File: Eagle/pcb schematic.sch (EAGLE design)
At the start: 17 parts

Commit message: PCB finita
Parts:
- BLUETOOTH: device SparkFun-Connectors:CONN_02 -> SparkFun-Connectors:CONN_04
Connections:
- net GND: now also BLUETOOTH.2
- net N$4: now also BLUETOOTH.4, PIN_123-124.1; no longer BLUETOOTH.1, PIN_123-124.2
- net N$6: now also BLUETOOTH.3, PIN_123-124.2; no longer BLUETOOTH.2, PIN_123-124.1
- net N$9: now also BLUETOOTH.1
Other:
- moved on the sheet: PIN_123-124
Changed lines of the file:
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@@
 <part name="R1" library="SparkFun-Resistors" deviceset="RESISTOR" device="AXIAL-0.3" value=" "/>
 <part name="PIN_123-124" library="SparkFun-Connectors" deviceset="CONN_02" device=""/>
-<part name="BLUETOOTH" library="SparkFun-Connectors" deviceset="CONN_02" device=""/>
 <part name="J1" library="SparkFun-Connectors" deviceset="CONN_02" device=""/>
+<part name="BLUETOOTH" library="SparkFun-Connectors" deviceset="CONN_04" device=""/>
 </parts>
 <sheets>
@@
 <attribute name="NAME" x="-10.16" y="61.976" size="1.778" layer="95" font="vector" rot="R180" align="bottom-center"/>
 </instance>
-<instance part="PIN_123-124" gate="G$1" x="-55.88" y="48.26" smashed="yes">
-<attribute name="VALUE" x="-58.42" y="43.434" size="1.778" layer="96" font="vector"/>
-<attribute name="NAME" x="-61.468" y="43.18" size="1.778" layer="95" font="vector" rot="R90"/>
-</instance>
-<instance part="BLUETOOTH" gate="G$1" x="-25.4" y="50.8" smashed="yes" rot="R180">
-<attribute name="VALUE" x="-22.86" y="55.626" size="1.778" layer="96" font="vector" rot="R180"/>
-<attribute name="NAME" x="-22.352" y="53.34" size="1.778" layer="95" font="vector" rot="R270"/>
+<instance part="PIN_123-124" gate="G$1" x="-55.88" y="45.72" smashed="yes">
+<attribute name="VALUE" x="-58.42" y="40.894" size="1.778" layer="96" font="vector"/>
+<attribute name="NAME" x="-61.468" y="40.64" size="1.778" layer="95" font="vector" rot="R90"/>
 </instance>
 <instance part="J1" gate="G$1" x="5.08" y="96.52" smashed="yes" rot="R270">
 <attribute name="VALUE" x="0.254" y="99.06" size="1.778" layer="96" font="vector" rot="R270"/>
 <attribute name="NAME" x="10.668" y="99.06" size="1.778" layer="95" font="vector" rot="R270"/>
+</instance>
+<instance part="BLUETOOTH" gate="G$1" x="17.78" y="50.8" smashed="yes" rot="R180">
+<attribute name="VALUE" x="22.86" y="58.166" size="1.778" layer="96" font="vector" rot="R180"/>
+<attribute name="NAME" x="23.368" y="55.88" size="1.778" layer="95" font="vector" rot="R270"/>
 </instance>
 </instances>
@@
 <wire x1="-48.26" y1="76.2" x2="5.08" y2="76.2" width="0.1524" layer="91"/>
 <pinref part="FLEX2" gate="G$1" pin="1"/>
-<wire x1="30.48" y1="76.2" x2="33.02" y2="76.2" width="0.1524" layer="91"/>
-<wire x1="33.02" y1="76.2" x2="45.72" y2="76.2" width="0.1524" layer="91"/>
 <wire x1="45.72" y1="20.32" x2="45.72" y2="76.2" width="0.1524" layer="91"/>
 <wire x1="45.72" y1="76.2" x2="60.96" y2="76.2" width="0.1524" layer="91"/>
@@
 <wire x1="60.96" y1="7.62" x2="60.96" y2="76.2" width="0.1524" layer="91"/>
 <junction x="60.96" y="76.2"/>
+<wire x1="5.08" y1="76.2" x2="12.7" y2="76.2" width="0.1524" layer="91"/>
+<junction x="5.08" y="76.2"/>
+<pinref part="BLUETOOTH" gate="G$1" pin="1"/>
+<wire x1="12.7" y1="76.2" x2="30.48" y2="76.2" width="0.1524" layer="91"/>
+<wire x1="30.48" y1="76.2" x2="45.72" y2="76.2" width="0.1524" layer="91"/>
+<wire x1="12.7" y1="53.34" x2="12.7" y2="76.2" width="0.1524" layer="91"/>
+<junction x="12.7" y="76.2"/>
 <pinref part="FLEX1" gate="G$1" pin="1"/>
 <wire x1="30.48" y1="35.56" x2="30.48" y2="76.2" width="0.1524" layer="91"/>
-<wire x1="5.08" y1="76.2" x2="30.48" y2="76.2" width="0.1524" layer="91"/>
-<junction x="5.08" y="76.2"/>
+<junction x="30.48" y="76.2"/>
 </segment>
 </net>
@@
 <pinref part="R1" gate="G$1" pin="2"/>
 <wire x1="-22.86" y1="63.5" x2="-15.24" y2="63.5" width="0.1524" layer="91"/>
-</segment>
-</net>
-<net name="N$4" class="0">
-<segment>
-<pinref part="PIN_123-124" gate="G$1" pin="2"/>
-<pinref part="BLUETOOTH" gate="G$1" pin="1"/>
-<wire x1="-48.26" y1="50.8" x2="-33.02" y2="50.8" width="0.1524" layer="91"/>
-</segment>
-</net>
-<net name="N$6" class="0">
-<segment>
-<pinref part="PIN_123-124" gate="G$1" pin="1"/>
-<pinref part="BLUETOOTH" gate="G$1" pin="2"/>
-<wire x1="-48.26" y1="48.26" x2="-33.02" y2="48.26" width="0.1524" layer="91"/>
 </segment>
 </net>
@@
 <pinref part="R5" gate="G$1" pin="2"/>
 <wire x1="27.94" y1="73.66" x2="27.94" y2="48.26" width="0.1524" layer="91"/>
-<wire x1="7.62" y1="73.66" x2="27.94" y2="73.66" width="0.1524" layer="91"/>
+<wire x1="7.62" y1="73.66" x2="10.16" y2="73.66" width="0.1524" layer="91"/>
 <junction x="27.94" y="73.66"/>
 <pinref part="R1" gate="G$1" pin="1"/>
+<wire x1="10.16" y1="73.66" x2="27.94" y2="73.66" width="0.1524" layer="91"/>
 <wire x1="-5.08" y1="63.5" x2="-5.08" y2="73.66" width="0.1524" layer="91"/>
 <wire x1="-48.26" y1="73.66" x2="-5.08" y2="73.66" width="0.1524" layer="91"/>
@@
 <junction x="7.62" y="73.66"/>
 <junction x="-5.08" y="73.66"/>
-</segment>
-</net>
+<pinref part="BLUETOOTH" gate="G$1" pin="2"/>
+<wire x1="12.7" y1="50.8" x2="10.16" y2="50.8" width="0.1524" layer="91"/>
+<wire x1="10.16" y1="50.8" x2="10.16" y2="73.66" width="0.1524" layer="91"/>
+<junction x="10.16" y="73.66"/>
+</segment>
+</net>
+<net name="N$4" class="0">
+<segment>
+<pinref part="PIN_123-124" gate="G$1" pin="1"/>
+<pinref part="BLUETOOTH" gate="G$1" pin="4"/>
+<wire x1="-48.26" y1="45.72" x2="12.7" y2="45.72" width="0.1524" layer="91"/>
+</segment>
+</net>
+<net name="N$6" class="0">
+<segment>
+<pinref part="PIN_123-124" gate="G$1" pin="2"/>
+<pinref part="BLUETOOTH" gate="G$1" pin="3"/>
+<wire x1="-48.26" y1="48.26" x2="12.7" y2="48.26" width="0.1524" layer="91"/>
+</segment>
+</net>

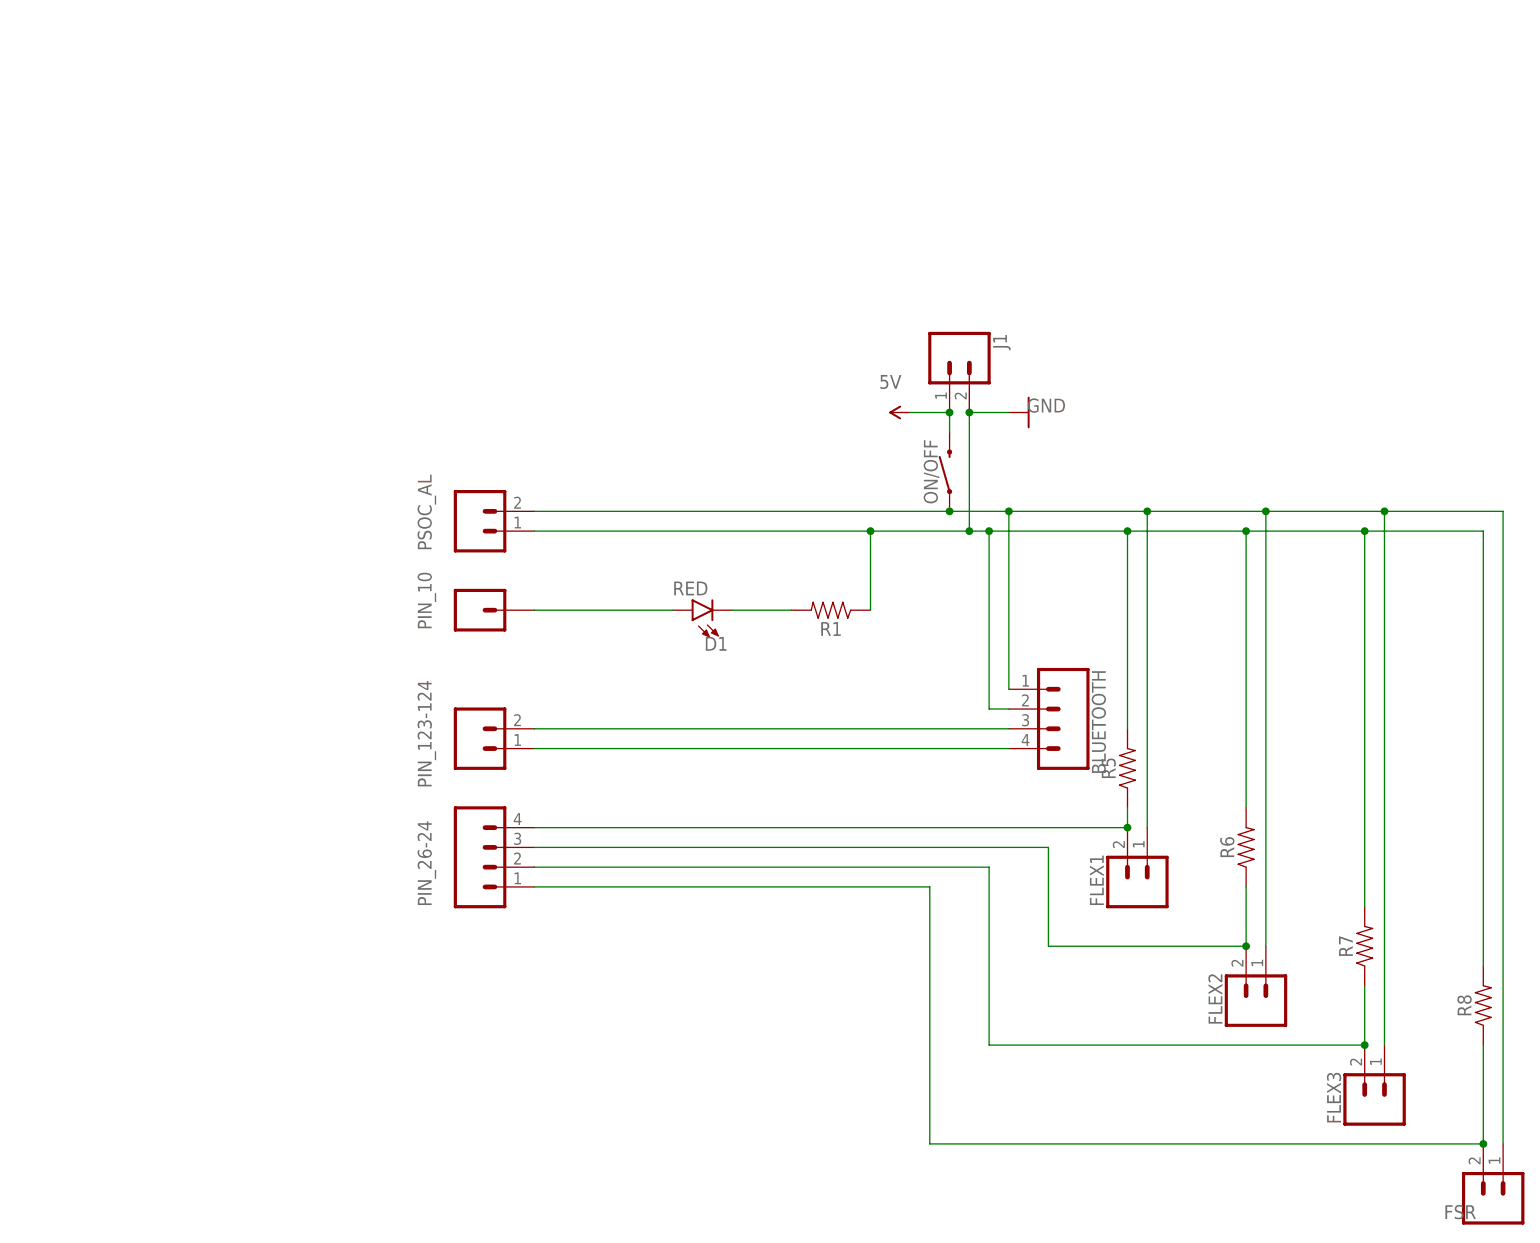
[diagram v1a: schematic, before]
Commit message: PCB modifica tracce e aggiunta componenti batteria
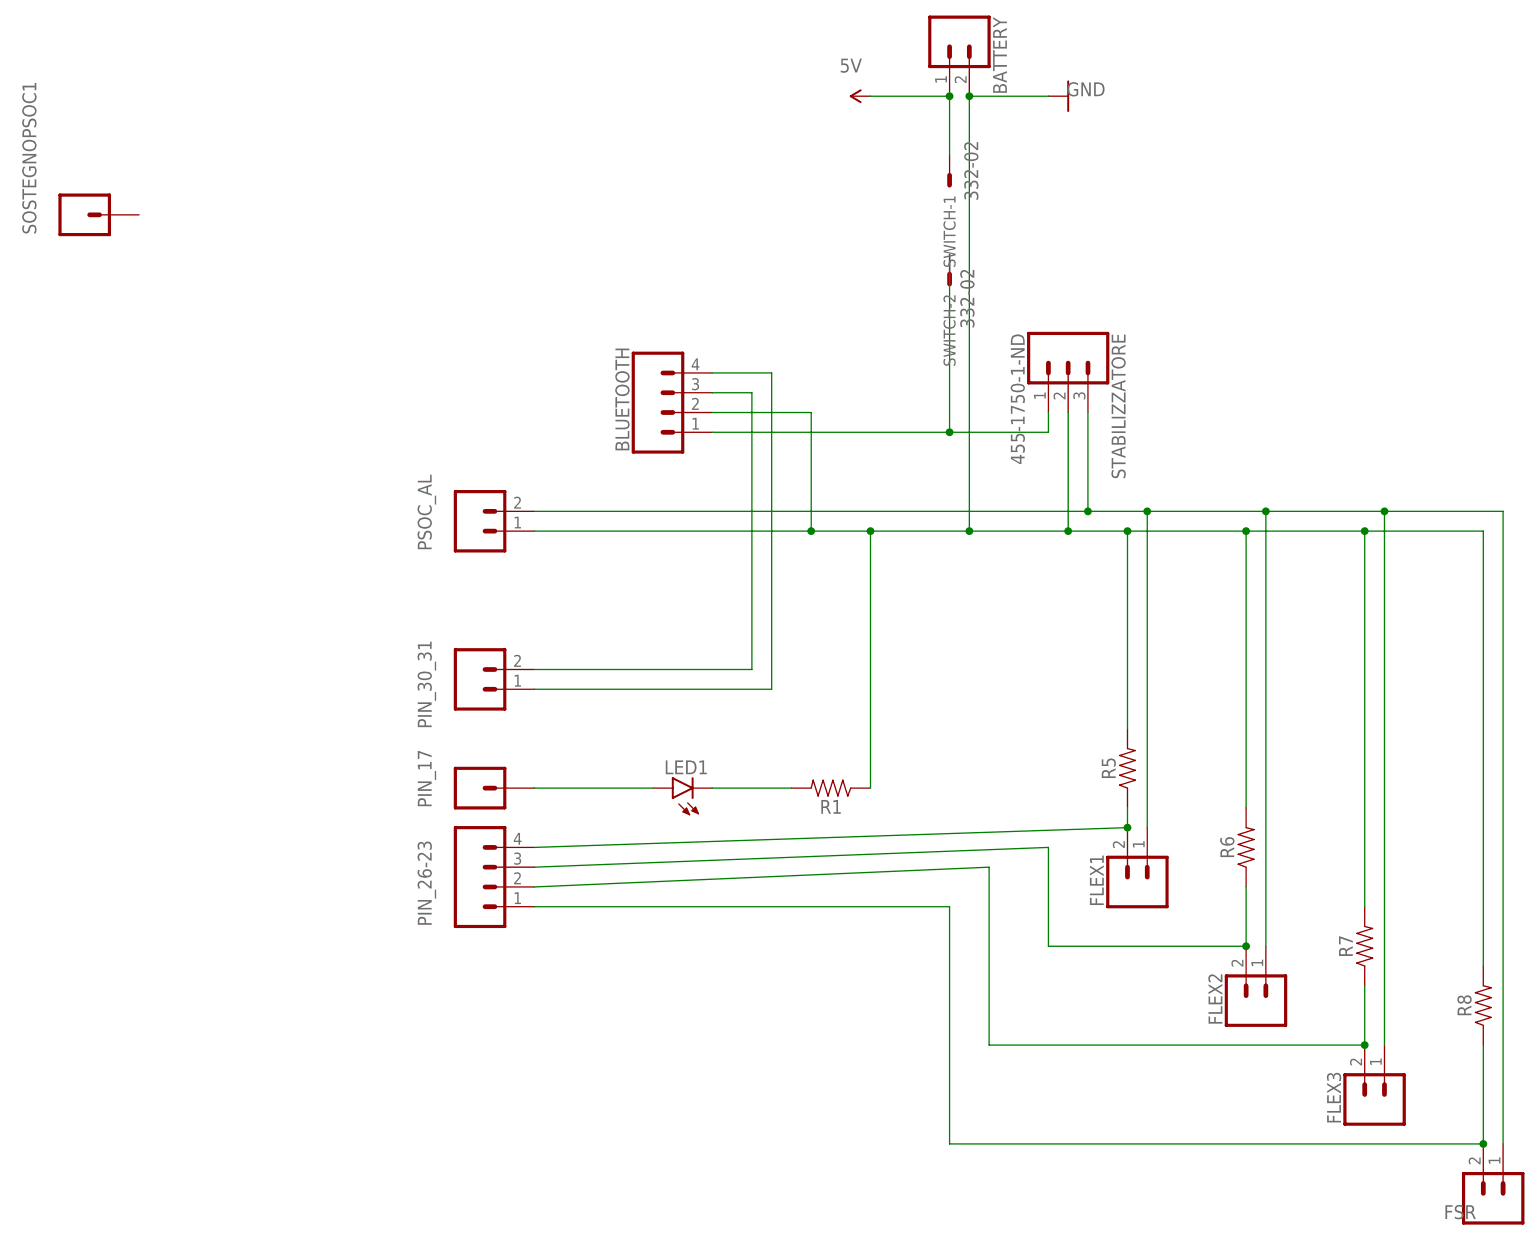
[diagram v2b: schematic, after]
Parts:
- removed D1: RED, SparkFun-LED:LED-RED0603
- removed J1, PIN_123-124: (no value), SparkFun-Connectors:CONN_02
- removed ON/OFF: MOMENTARY-SWITCH-SPST-SMD-6.0X3.5MM, SparkFun-Switches:MOMENTARY-SWITCH-SPST-SMD-6.0X3.5MM
- removed PIN_10: (no value), SparkFun-Connectors:CONN_01
- removed PIN_26-24: (no value), SparkFun-Connectors:CONN_04
- added BATTERY, PIN_30_31: (no value), SparkFun-Connectors:CONN_02
- added LED1: (no value), led:LED5MM
- added PIN_17, SOSTEGNOPSOC1: (no value), SparkFun-Connectors:CONN_01
- added PIN_26-23: (no value), SparkFun-Connectors:CONN_04
- added STABILIZZATORE: 455-1750-1-ND, SparkFun-Connectors:CONN_03
- added SWITCH: 332-02, con-garry:332-02
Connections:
- removed net N$11: D1.C, R1.2
- removed net N$9: BLUETOOTH.1, FLEX1.1, FLEX2.1, FLEX3.1, FSR.1, ON/OFF.1, PSOC_AL.2
- new net N$12: FLEX1.1, FLEX2.1, FLEX3.1, FSR.1, PSOC_AL.2, STABILIZZATORE.3
- new net N$7: LED1.A, PIN_17.1
- new net N$8: LED1.C, R1.2
- net 5V: now also BATTERY.1, SWITCH-1.S; no longer J1.1, ON/OFF.2
- net GND: now also BATTERY.2, STABILIZZATORE.2; no longer J1.2
- net N$1: now also PIN_26-23.4; no longer PIN_26-24.4
- net N$10: now also BLUETOOTH.1, STABILIZZATORE.1, SWITCH-2.S; no longer D1.A, PIN_10.1
- net N$2: now also PIN_26-23.3; no longer PIN_26-24.3
- net N$3: now also PIN_26-23.2; no longer PIN_26-24.2
- net N$4: now also BLUETOOTH.3, PIN_30_31.2; no longer BLUETOOTH.4, PIN_123-124.1
- net N$5: now also PIN_26-23.1; no longer PIN_26-24.1
- net N$6: now also BLUETOOTH.4, PIN_30_31.1; no longer BLUETOOTH.3, PIN_123-124.2
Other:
- moved on the sheet: BLUETOOTH, R1
